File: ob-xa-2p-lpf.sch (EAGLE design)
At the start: 35 parts, among them IC1 AS3320

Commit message: draft
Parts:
- removed R19: 10k, pot:TRIM_US-B64Y
- removed R6: 500k, pot:TRIM_US-B64Y
- added C10, C11, C12, C13: 100n, rcl:CPOL-EUE1.8-4
- added C7, C9: 100n, rcl:C-EU050-025X075
- added C8: 10u, rcl:CPOL-EUE1.8-4
- added IC2: (no value), linear:7905T
- added POWER_IN: (no value), pinhead:PINHD-1X4
- added R22: 47, rcl:R-US_0207/10
- added RES_ADJ: 500k, pot:TRIM_US-S63P
- added V/OCT_ADJ: 10k, pot:TRIM_US-S63P
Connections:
- new net -15V: C12.-, POWER_IN.4, R22.2
- new net N$21: C7.2, C8.-, IC2.VI, R22.1
- net +15V: now also C10.+, C13.+, POWER_IN.1
- net -5V: now also C11.-, C9.2, IC2.VO
- net 0V: now also C10.-, C11.+, C12.+, C13.-, C7.1, C8.+, C9.1, IC2.GND, POWER_IN.2, POWER_IN.3
- net FREQ_CV: now also V/OCT_ADJ.E, V/OCT_ADJ.S; no longer R19.S
- net N$15: now also RES_ADJ.E, RES_ADJ.S; no longer R6.S
- net N$2: now also V/OCT_ADJ.A; no longer R19.A
- net VIN: now also RES_ADJ.A; no longer R6.A
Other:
- note added: "LM7905"
- note added: "Note: output capacitance less than 7905 datasheet."
- moved on the sheet: FREQ_CV, R15, R20, R21

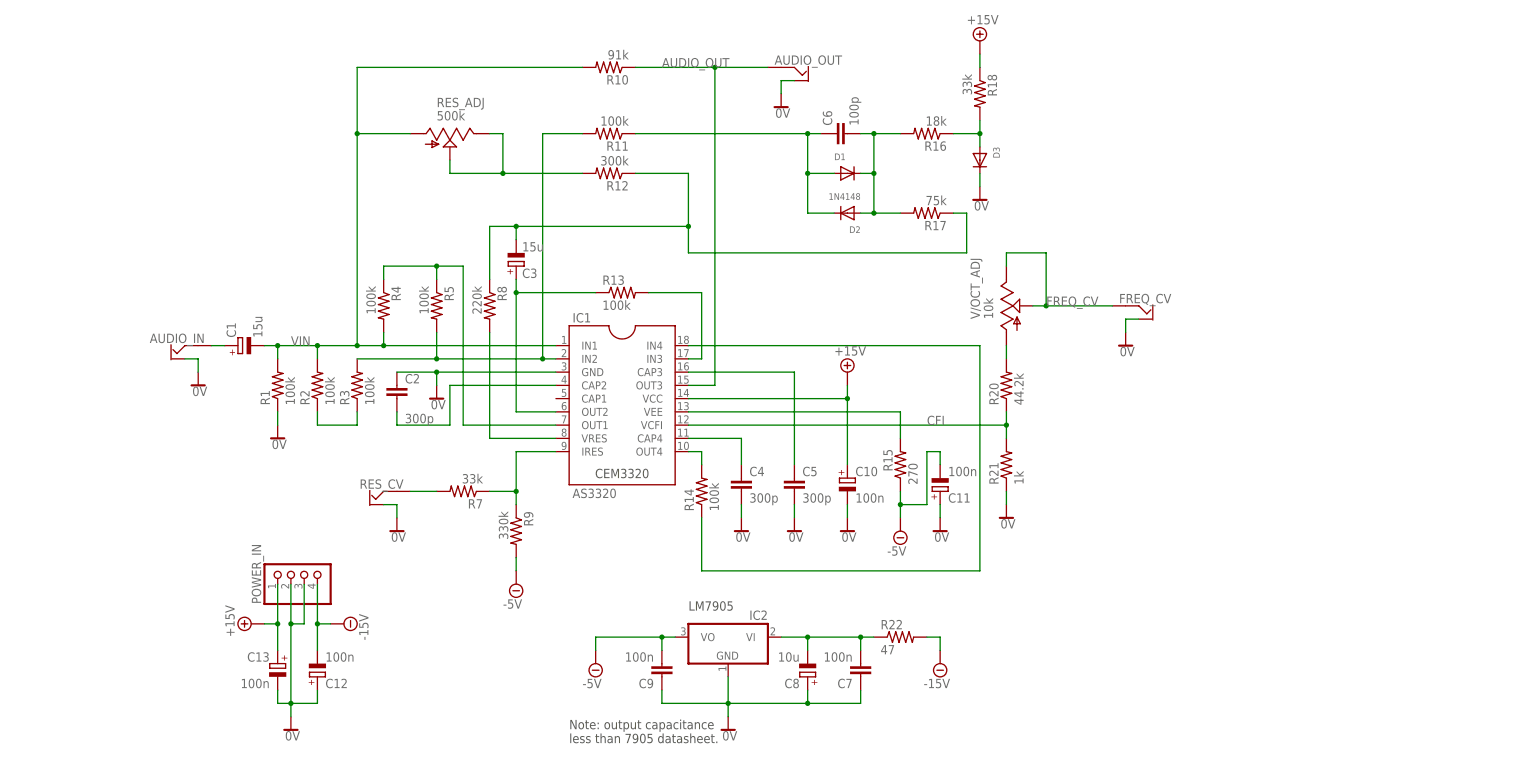
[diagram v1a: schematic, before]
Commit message: add cv imput
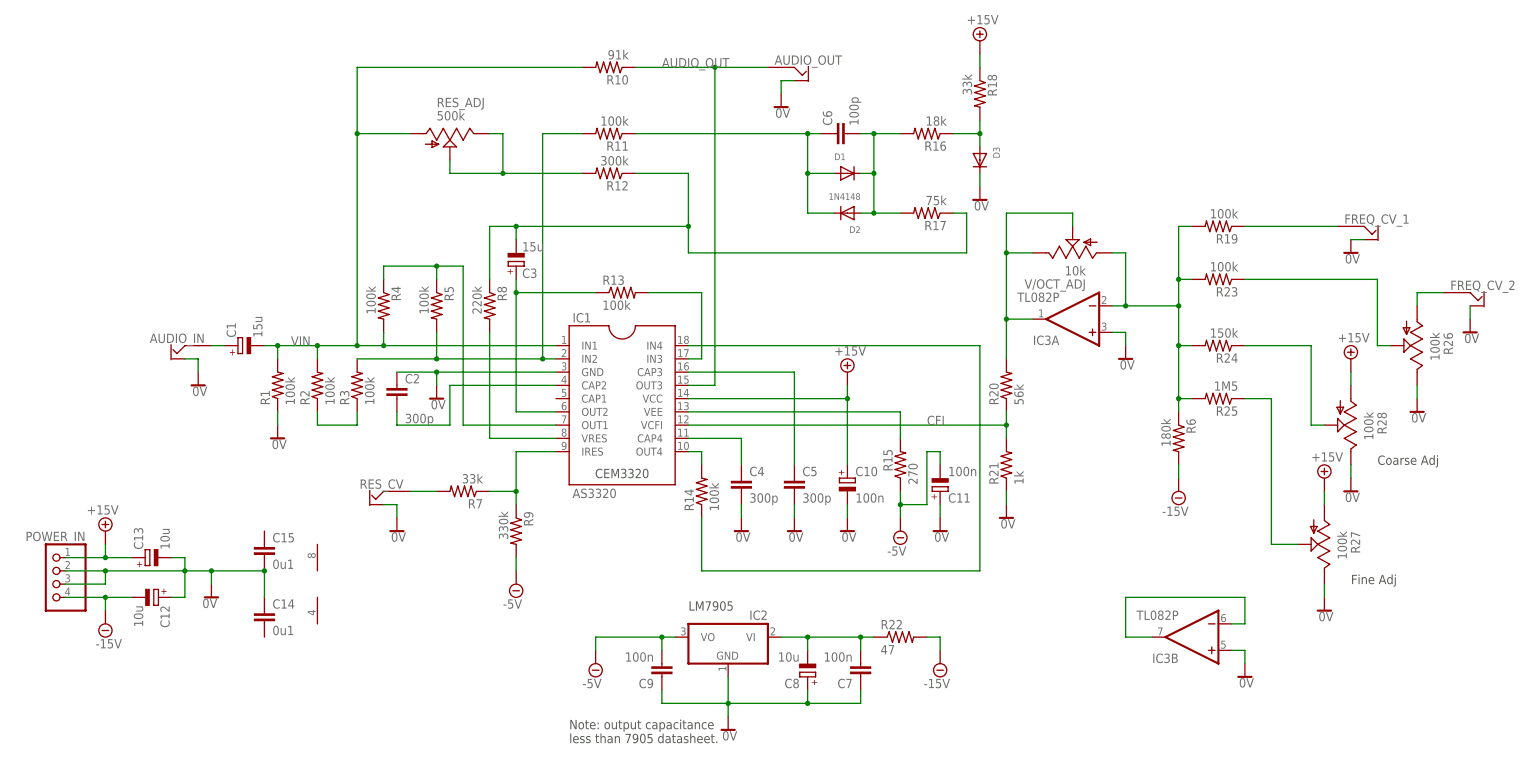
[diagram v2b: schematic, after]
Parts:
- removed FREQ_CV: OFFBOARD2JACKALT, aarons_library:OFFBOARD2JACKALT
- added C14, C15: 0u1, rcl:C-EU050-025X075
- added FREQ_CV_1, FREQ_CV_2: OFFBOARD2JACKALT, aarons_library:OFFBOARD2JACKALT
- added IC3: TL082P, linear:TL082P
- added R19, R23: 100k, rcl:R-US_0207/10
- added R24: 150k, rcl:R-US_0207/10
- added R25: 1M5, rcl:R-US_0207/10
- added R26, R27, R28: 100k, pot:TRIM_US-B64Y
- added R6: 180k, rcl:R-US_0207/10
- C12, C13: value 100n -> 10u
- R20: value 44.2k -> 56k
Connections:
- removed net FREQ_CV: FREQ_CV.SIGNAL, V/OCT_ADJ.E, V/OCT_ADJ.S
- new net N$22: IC3B.-IN, IC3B.OUT
- new net N$23: IC3A.-IN, R19.2, R23.2, R24.2, R25.2, R6.1, V/OCT_ADJ.A
- new net N$24: FREQ_CV_1.SIGNAL, R19.1
- new net N$25: R23.1, R26.S
- new net N$26: FREQ_CV_2.SIGNAL, R26.A
- new net N$27: R24.1, R28.S
- new net N$28: R25.1, R27.S
- net +15V: now also R27.A, R28.A
- net -15V: now also R6.2
- net 0V: now also C14.1, C15.2, FREQ_CV_1.GND, FREQ_CV_2.GND, IC3A.+IN, IC3B.+IN, R26.E, R27.E, R28.E; no longer FREQ_CV.GND
- net N$2: now also IC3A.OUT, V/OCT_ADJ.E, V/OCT_ADJ.S; no longer V/OCT_ADJ.A
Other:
- note added: "Coarse Adj"
- note added: "Fine Adj"
- moved on the sheet: C12, C13, POWER_IN, V/OCT_ADJ

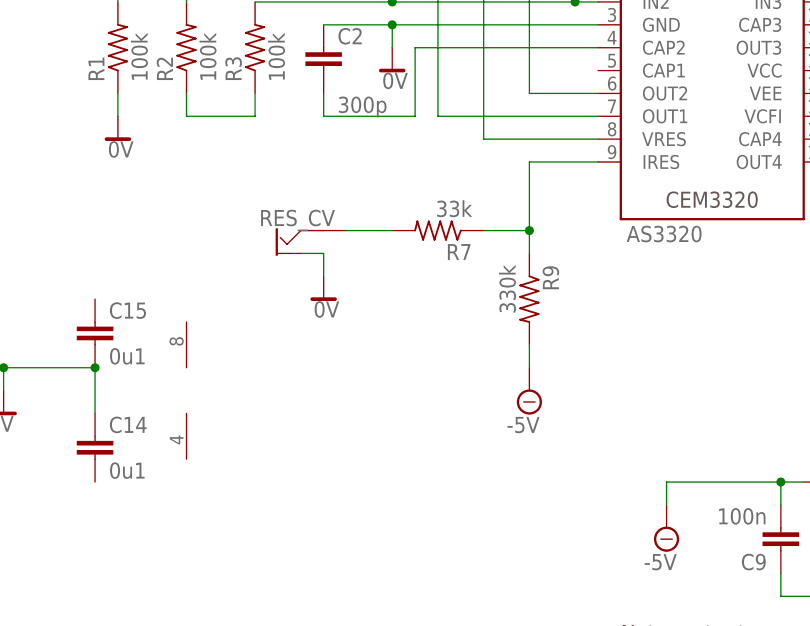
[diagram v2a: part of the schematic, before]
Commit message: add res ctrl
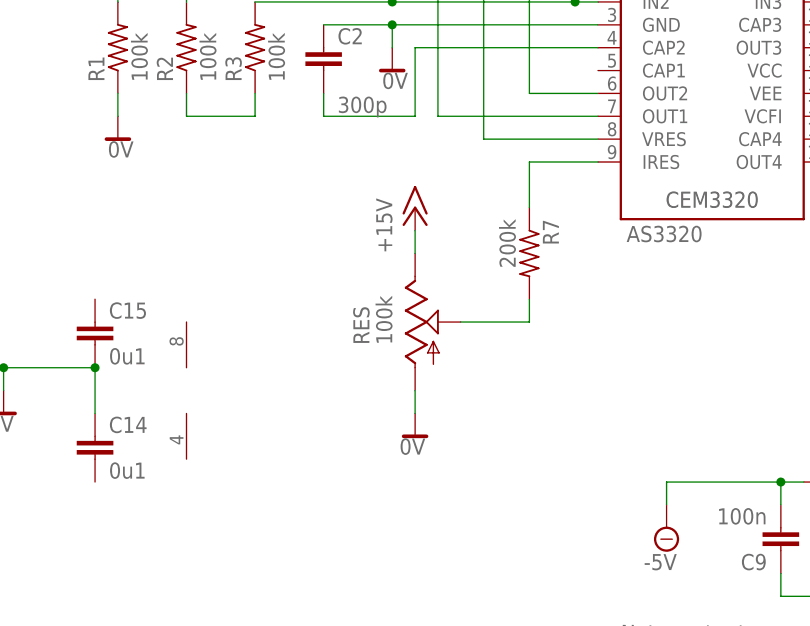
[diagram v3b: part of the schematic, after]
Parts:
- removed R9: 330k, rcl:R-US_0207/10
- removed RES_CV: OFFBOARD2JACKALT, aarons_library:OFFBOARD2JACKALT
- added RES: 100k, pot:TRIM_US-B64Y
- R7: value 33k -> 200k
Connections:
- net +15V: now also RES.E
- net -5V: no longer R9.2
- net 0V: now also RES.A; no longer RES_CV.GND
- net N$17: no longer R9.1
- net N$19: now also RES.S; no longer RES_CV.SIGNAL
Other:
- moved on the sheet: R7
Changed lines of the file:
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@@
 <part name="R16" library="rcl" library_urn="urn:adsk.eagle:library:334" deviceset="R-US_" device="0207/10" package3d_urn="urn:adsk.eagle:package:23491/2" value="18k"/>
 <part name="R10" library="rcl" library_urn="urn:adsk.eagle:library:334" deviceset="R-US_" device="0207/10" package3d_urn="urn:adsk.eagle:package:23491/2" value="91k"/>
-<part name="R7" library="rcl" library_urn="urn:adsk.eagle:library:334" deviceset="R-US_" device="0207/10" package3d_urn="urn:adsk.eagle:package:23491/2" value="33k"/>
+<part name="R7" library="rcl" library_urn="urn:adsk.eagle:library:334" deviceset="R-US_" device="0207/10" package3d_urn="urn:adsk.eagle:package:23491/2" value="200k"/>
 <part name="R18" library="rcl" library_urn="urn:adsk.eagle:library:334" deviceset="R-US_" device="0207/10" package3d_urn="urn:adsk.eagle:package:23491/2" value="33k"/>
 <part name="R8" library="rcl" library_urn="urn:adsk.eagle:library:334" deviceset="R-US_" device="0207/10" package3d_urn="urn:adsk.eagle:package:23491/2" value="220k"/>
@@
 <part name="R11" library="rcl" library_urn="urn:adsk.eagle:library:334" deviceset="R-US_" device="0207/10" package3d_urn="urn:adsk.eagle:package:23491/2" value="100k"/>
 <part name="R15" library="rcl" library_urn="urn:adsk.eagle:library:334" deviceset="R-US_" device="0207/10" package3d_urn="urn:adsk.eagle:package:23491/2" value="270"/>
-<part name="R9" library="rcl" library_urn="urn:adsk.eagle:library:334" deviceset="R-US_" device="0207/10" package3d_urn="urn:adsk.eagle:package:23491/2" value="330k"/>
-<part name="SUPPLY5" library="supply2" library_urn="urn:adsk.eagle:library:372" deviceset="-5V" device=""/>
-<part name="RES_CV" library="aarons_library" deviceset="OFFBOARD2JACKALT" device=""/>
-<part name="SUPPLY3" library="supply2" library_urn="urn:adsk.eagle:library:372" deviceset="0V" device=""/>
 <part name="C4" library="rcl" library_urn="urn:adsk.eagle:library:334" deviceset="C-EU" device="050-025X075" package3d_urn="urn:adsk.eagle:package:23637/1" value="300p"/>
 <part name="C5" library="rcl" library_urn="urn:adsk.eagle:library:334" deviceset="C-EU" device="050-025X075" package3d_urn="urn:adsk.eagle:package:23637/1" value="300p"/>
@@
 <part name="C14" library="rcl" library_urn="urn:adsk.eagle:library:334" deviceset="C-EU" device="050-025X075" package3d_urn="urn:adsk.eagle:package:23637/1" value="0u1"/>
 <part name="C15" library="rcl" library_urn="urn:adsk.eagle:library:334" deviceset="C-EU" device="050-025X075" package3d_urn="urn:adsk.eagle:package:23637/1" value="0u1"/>
+<part name="SUPPLY3" library="supply2" library_urn="urn:adsk.eagle:library:372" deviceset="0V" device=""/>
+<part name="RES" library="pot" library_urn="urn:adsk.eagle:library:331" deviceset="TRIM_US-" device="B64Y" package3d_urn="urn:adsk.eagle:package:22690/1" value="100k"/>
+<part name="P+1" library="supply1" library_urn="urn:adsk.eagle:library:371" deviceset="+15V" device=""/>
 </parts>
 <sheets>
@@
 <attribute name="VALUE" x="87.63" y="97.282" size="1.778" layer="96" rot="R180"/>
 </instance>
-<instance part="R7" gate="G$1" x="55.88" y="12.7" smashed="yes" rot="R180">
-<attribute name="NAME" x="59.69" y="11.2014" size="1.778" layer="95" rot="R180"/>
-<attribute name="VALUE" x="59.69" y="16.002" size="1.778" layer="96" rot="R180"/>
+<instance part="R7" gate="G$1" x="66.04" y="10.16" smashed="yes" rot="R270">
+<attribute name="NAME" x="67.5386" y="13.97" size="1.778" layer="95" rot="R270"/>
+<attribute name="VALUE" x="62.738" y="13.97" size="1.778" layer="96" rot="R270"/>
 </instance>
 <instance part="R18" gate="G$1" x="154.94" y="88.9" smashed="yes" rot="R270">
@@
 <attribute name="VALUE" x="143.002" y="13.97" size="1.778" layer="96" rot="R90"/>
 </instance>
-<instance part="R9" gate="G$1" x="66.04" y="5.08" smashed="yes" rot="R270">
-<attribute name="NAME" x="67.5386" y="8.89" size="1.778" layer="95" rot="R270"/>
-<attribute name="VALUE" x="62.738" y="8.89" size="1.778" layer="96" rot="R270"/>
-</instance>
-<instance part="SUPPLY5" gate="-5V" x="66.04" y="-5.08" smashed="yes">
-<attribute name="VALUE" x="63.5" y="-9.779" size="1.778" layer="96"/>
-</instance>
-<instance part="RES_CV" gate="G$1" x="40.64" y="10.16" smashed="yes" rot="MR0">
-<attribute name="NAME" x="44.45" y="13.208" size="1.778" layer="95" rot="MR0"/>
-</instance>
-<instance part="SUPPLY3" gate="0V" x="43.18" y="5.08" smashed="yes">
-<attribute name="VALUE" x="42.037" y="3.048" size="1.778" layer="96"/>
-</instance>
 <instance part="C4" gate="G$1" x="109.22" y="15.24" smashed="yes">
 <attribute name="NAME" x="110.744" y="15.621" size="1.778" layer="95"/>
@@
 <attribute name="NAME" x="19.304" y="2.921" size="1.778" layer="95"/>
 <attribute name="VALUE" x="19.304" y="-2.159" size="1.778" layer="96"/>
+</instance>
+<instance part="SUPPLY3" gate="0V" x="53.34" y="-10.16" smashed="yes" rot="MR0">
+<attribute name="VALUE" x="54.483" y="-12.192" size="1.778" layer="96" rot="MR0"/>
+</instance>
+<instance part="RES" gate="G$1" x="53.34" y="2.54" smashed="yes">
+<attribute name="NAME" x="48.26" y="0" size="1.778" layer="95" rot="R90"/>
+<attribute name="VALUE" x="50.8" y="0" size="1.778" layer="96" rot="R90"/>
+</instance>
+<instance part="P+1" gate="1" x="53.34" y="15.24" smashed="yes">
+<attribute name="VALUE" x="50.8" y="10.16" size="1.778" layer="96" rot="R90"/>
 </instance>
 </instances>
@@
 <wire x1="116.84" y1="91.44" x2="116.84" y2="88.9" width="0.1524" layer="91"/>
 <pinref part="SUPPLY7" gate="0V" pin="0V"/>
-</segment>
-<segment>
-<pinref part="RES_CV" gate="G$1" pin="GND"/>
-<pinref part="SUPPLY3" gate="0V" pin="0V"/>
-<wire x1="40.64" y1="10.16" x2="43.18" y2="10.16" width="0.1524" layer="91"/>
-<wire x1="43.18" y1="10.16" x2="43.18" y2="7.62" width="0.1524" layer="91"/>
 </segment>
 <segment>
@@
 <pinref part="SUPPLY29" gate="0V" pin="0V"/>
 <wire x1="220.98" y1="-7.62" x2="220.98" y2="-5.08" width="0.1524" layer="91"/>
+</segment>
+<segment>
+<pinref part="RES" gate="G$1" pin="A"/>
+<pinref part="SUPPLY3" gate="0V" pin="0V"/>
+<wire x1="53.34" y1="-7.62" x2="53.34" y2="-5.08" width="0.1524" layer="91"/>
 </segment>
 </net>
@@
 <wire x1="220.98" y1="12.7" x2="220.98" y2="10.16" width="0.1524" layer="91"/>
 </segment>
+<segment>
+<pinref part="RES" gate="G$1" pin="E"/>
+<wire x1="53.34" y1="12.7" x2="53.34" y2="10.16" width="0.1524" layer="91"/>
+<pinref part="P+1" gate="1" pin="+15V"/>
+</segment>
 </net>
 <net name="N$10" class="0">
@@
 </segment>
 <segment>
-<pinref part="R9" gate="G$1" pin="2"/>
-<pinref part="SUPPLY5" gate="-5V" pin="-5V"/>
-<wire x1="66.04" y1="0" x2="66.04" y2="-2.54" width="0.1524" layer="91"/>
-</segment>
-<segment>
 <pinref part="IC2" gate="A1" pin="VO"/>
 <wire x1="96.52" y1="-15.24" x2="93.98" y2="-15.24" width="0.1524" layer="91"/>
@@
 <net name="N$17" class="0">
 <segment>
-<pinref part="R7" gate="G$1" pin="1"/>
-<wire x1="60.96" y1="12.7" x2="66.04" y2="12.7" width="0.1524" layer="91"/>
-<pinref part="R9" gate="G$1" pin="1"/>
-<wire x1="66.04" y1="12.7" x2="66.04" y2="10.16" width="0.1524" layer="91"/>
 <pinref part="IC1" gate="G$1" pin="IRES"/>
 <wire x1="73.66" y1="20.32" x2="66.04" y2="20.32" width="0.1524" layer="91"/>
-<wire x1="66.04" y1="20.32" x2="66.04" y2="12.7" width="0.1524" layer="91"/>
-<junction x="66.04" y="12.7"/>
-</segment>
-</net>
-<net name="N$19" class="0">
-<segment>
-<pinref part="R7" gate="G$1" pin="2"/>
-<pinref part="RES_CV" gate="G$1" pin="SIGNAL"/>
-<wire x1="50.8" y1="12.7" x2="45.72" y2="12.7" width="0.1524" layer="91"/>
+<pinref part="R7" gate="G$1" pin="1"/>
+<wire x1="66.04" y1="15.24" x2="66.04" y2="20.32" width="0.1524" layer="91"/>
 </segment>
 </net>
@@
 </segment>
 </net>
+<net name="N$19" class="0">
+<segment>
+<pinref part="RES" gate="G$1" pin="S"/>
+<wire x1="58.42" y1="2.54" x2="66.04" y2="2.54" width="0.1524" layer="91"/>
+<pinref part="R7" gate="G$1" pin="2"/>
+<wire x1="66.04" y1="2.54" x2="66.04" y2="5.08" width="0.1524" layer="91"/>
+</segment>
+</net>
